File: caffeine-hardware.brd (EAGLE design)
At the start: 65 x 56.5 mm, 31 parts, among them K1 PIN20X2, U1 EEPROM24

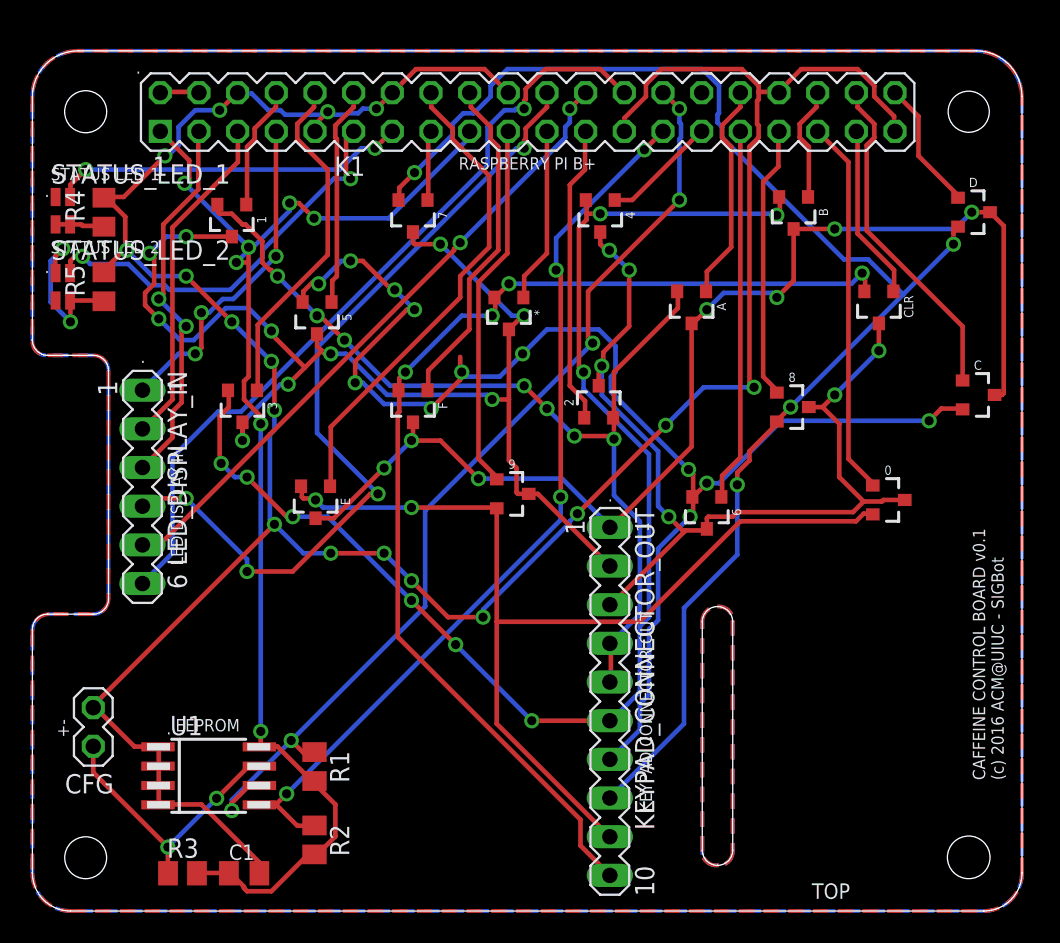
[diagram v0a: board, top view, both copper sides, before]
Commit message: using decoders
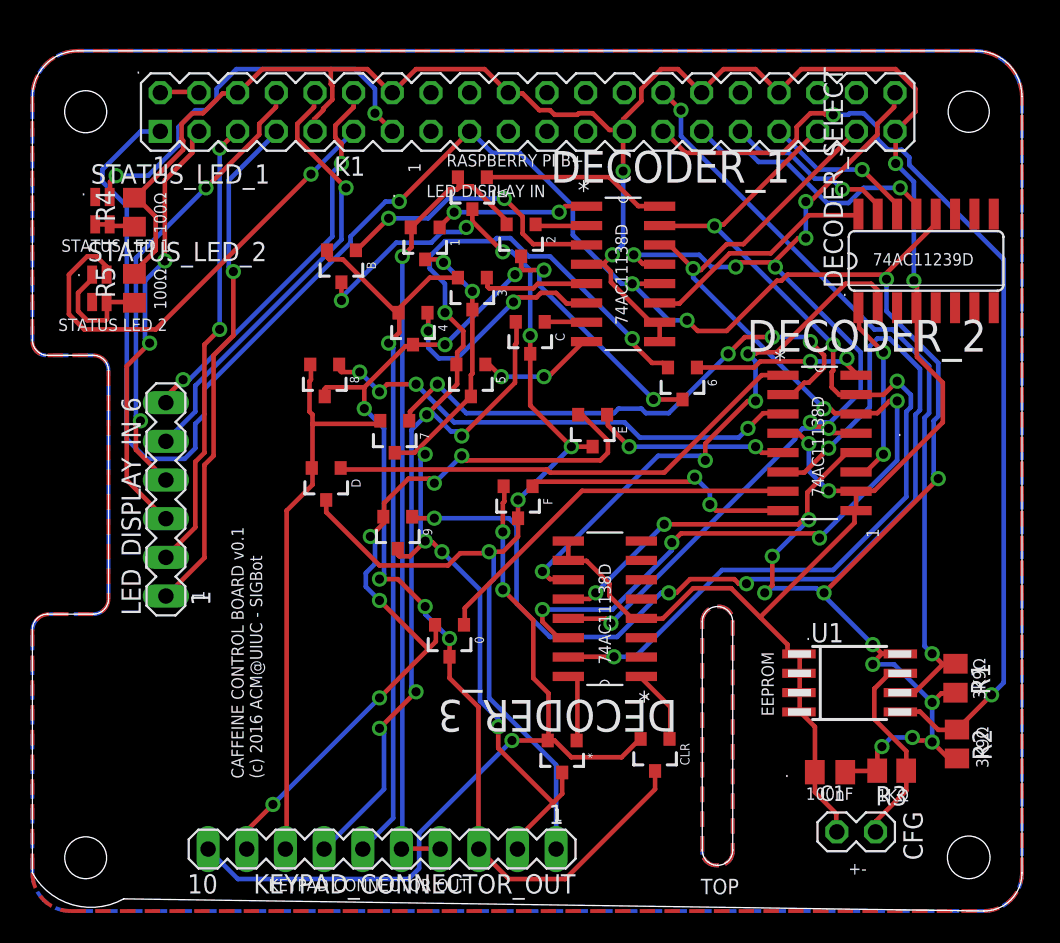
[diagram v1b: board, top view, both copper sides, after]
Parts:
- added DECODER_1, DECODER_2, DECODER_3: 74AC11138D, Texas Instruments_By_element14_Batch_1:SOIC127P600X175-16N
- added DECODER_SELECT: 74AC11239D, 74ac-logic:SO16
- moved CFG 51.7 mm to (55.4, 5.20), turned to 270 degrees
- moved R3 47.1 mm to (56.4, 9.22), turned to 180 degrees
- moved D 46.1 mm to (19.3, 28.1), turned to 180 degrees
- moved R2 42.7 mm to (60.7, 11.0)
- moved U1 42.5 mm to (53.7, 15.0)
- moved R1 42.5 mm to (60.6, 15.3)
- moved C1 39.0 mm to (52.4, 9.12), turned to 180 degrees
- moved CLR 32.9 mm to (40.9, 10.3)
- moved 8 30.8 mm to (19.2, 34.9), turned to 180 degrees
- moved 0 30.2 mm to (27.4, 17.8), turned to 180 degrees
- moved B 29.9 mm to (20.3, 42.4)
- moved C 29.6 mm to (32.7, 37.7), turned to 180 degrees
- moved * 29.3 mm to (34.8, 10.2)
- moved E 18.8 mm to (36.8, 31.6)
- moved KEYPAD_CONNECTOR_OUT 17.8 mm to (23.0, 4.07), turned to 180 degrees
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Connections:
- removed net N$21: 9.1, K1.19
- removed net N$8 (its old number): CLR.1, K1.37
- new net N$10: DECODER_1.11, DECODER_SELECT.16
- new net N$43: 6.1, DECODER_2.16
- new net N$44: D.1, DECODER_2.1
- new net N$45: 7.1, DECODER_2.2
- new net N$46: 8.1, DECODER_2.3
- new net N$47: DECODER_2.5, E.1
- new net N$48: 9.1, DECODER_2.6
- new net N$49: 0.1, DECODER_2.7
- new net N$50: DECODER_2.8, F.1
- new net N$51: *.1, DECODER_3.16
- new net N$52: CLR.1, DECODER_3.1
- net +3V3: now also DECODER_1.12, DECODER_2.12, DECODER_3.12, DECODER_SELECT.12
- net GND: now also DECODER_1.10, DECODER_1.4, DECODER_1.9, DECODER_2.10, DECODER_2.4, DECODER_2.9, DECODER_3.10, DECODER_3.4, DECODER_3.9, DECODER_SELECT.4
- net N$14: now also DECODER_SELECT.14, K1.33; no longer 0.1, K1.35
- net N$15: now also DECODER_1.15, DECODER_2.15, DECODER_3.15, K1.35; no longer 8.1, K1.33
- net N$16: now also DECODER_1.14, DECODER_2.14, DECODER_3.14, K1.37; no longer 6.1, K1.31
- net N$17: now also DECODER_1.13, DECODER_2.13, DECODER_3.13, K1.40; no longer 4.1, K1.29
- net N$18: now also DECODER_SELECT.15, K1.31; no longer 2.1, K1.23
- net N$19: now also DECODER_2.11, DECODER_SELECT.1; no longer 7.1, K1.15
- net N$20: now also DECODER_3.11, DECODER_SELECT.2; no longer *.1, K1.21
- net N$22: now also DECODER_SELECT.13, K1.29; no longer 1.1, K1.8
- net N$23: now also A.1, DECODER_1.16; no longer 3.1, K1.10
- net N$24: now also 1.1, DECODER_1.1; no longer 5.1, K1.12
- net N$25: now also 2.1, DECODER_1.2; no longer F.1, K1.18
- net N$26: now also B.1, DECODER_1.3; no longer E.1, K1.16
- net N$27: now also 3.1, DECODER_1.5; no longer A.1, K1.32
- net N$28: now also 4.1, DECODER_1.6; no longer B.1, K1.36
- net N$29: now also DECODER_1.7; no longer K1.38
- net N$30: now also 5.1, DECODER_1.8; no longer D.1, K1.40
- net N$33: now also K1.8; no longer K1.22
- net N$35: now also K1.12; no longer K1.26
- net N$36: now also K1.10; no longer K1.24
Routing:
- net +3V3: track 85.1 -> 186.5 mm, vias 7 -> 17
- net N$48: track 0.00 -> 68.0 mm, vias 0 -> 4
- net N$17: track 7.76 -> 67.7 mm, vias 0 -> 8
- net N$8: track 93.1 -> 37.5 mm, vias 4 -> 0
- net N$15: track 18.2 -> 66.4 mm, vias 0 -> 4
- net N$16: track 24.6 -> 70.3 mm, vias 0 -> 6
- net N$13: track 89.3 -> 48.2 mm, vias 9 -> 1
- net N$45: track 0.00 -> 36.5 mm, vias 0 -> 4
- net N$46: track 0.00 -> 32.5 mm, vias 0 -> 4
- net N$44: track 0.00 -> 31.9 mm
- net N$35: track 52.1 -> 26.0 mm, vias 1 -> 2
- net N$49: track 0.00 -> 25.2 mm
- net N$20: track 11.6 -> 36.5 mm, vias 0 -> 4
- net N$5: track 78.7 -> 53.8 mm, vias 10 -> 6
- net N$33: track 54.8 -> 30.3 mm, vias 4 -> 2
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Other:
- outline, holes or cut-outs redrawn
- board text added: "100nF"
- board text added: "100Ω"
- board text added: "1KΩ"
- board text added: "3K9Ω"
- board text added: "74AC11138D"
- board text added: "74AC11239D"

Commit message: using n channel
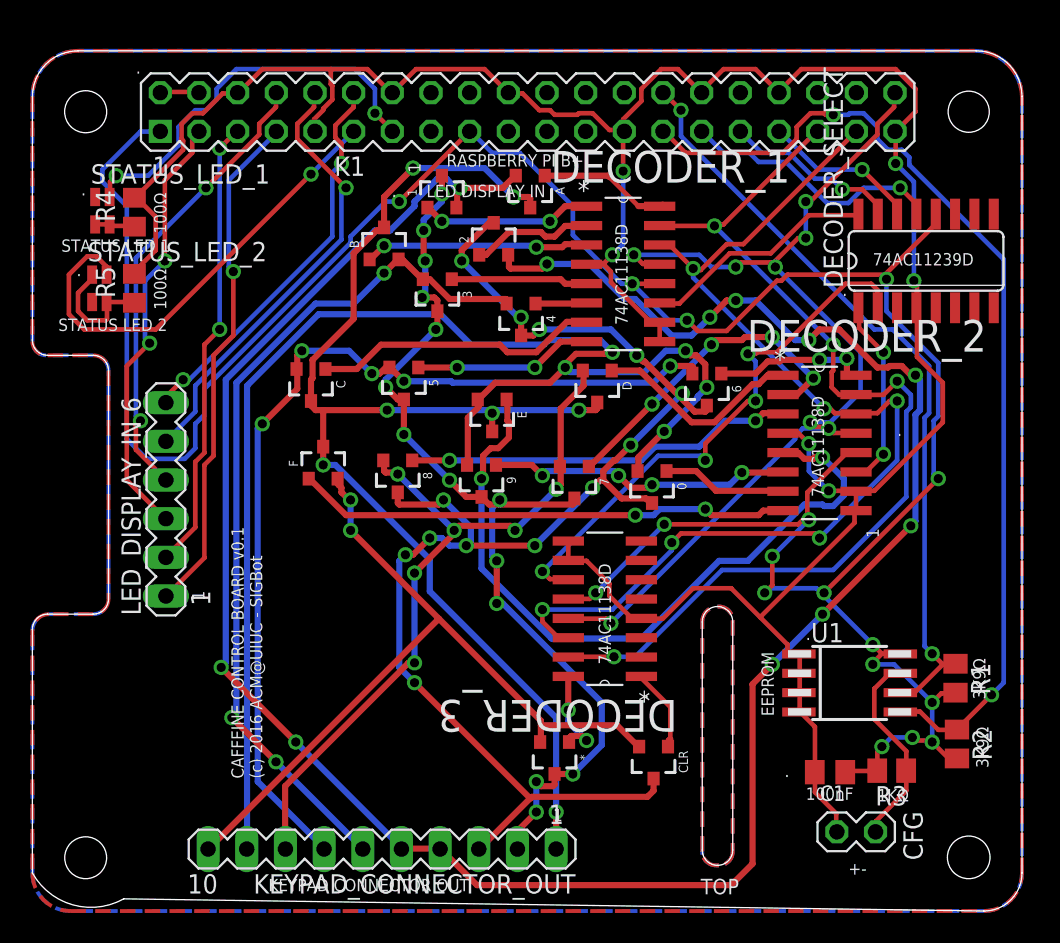
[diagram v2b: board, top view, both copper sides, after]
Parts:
- *, 0, 1, 2, 3, 4, 5, 6, 7, 8, 9, A, B, C, CLR, D, E, F: value BSS84L -> BSS138_F085
- moved D 18.9 mm to (37.1, 34.5)
- moved 0 16.7 mm to (40.7, 27.9)
- moved C 14.7 mm to (18.3, 34.6)
- moved F 13.0 mm to (19.1, 29.4), turned to 0 degrees
- moved 7 12.2 mm to (35.6, 28.2)
- moved 8 7.92 mm to (24.0, 28.6)
- moved 4 7.13 mm to (32.1, 38.9)
- moved E 6.68 mm to (30.2, 32.6)
- moved 9 6.47 mm to (29.5, 28.3)
- moved 5 4.40 mm to (24.4, 34.7)
- moved A 3.80 mm to (32.7, 47.3)
- moved 1 3.48 mm to (26.9, 47.2), turned to 0 degrees
- moved B 3.13 mm to (23.1, 43.8), turned to 0 degrees
- moved 3 2.30 mm to (26.6, 40.5)
- moved 2 1.80 mm to (30.3, 44.1), turned to 0 degrees
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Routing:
- net N$9: track 53.1 -> 157.3 mm, vias 1 -> 11
- net N$48: track 68.0 -> 20.1 mm
- net N$11: track 52.0 -> 91.8 mm, vias 6 -> 5
- net N$47: track 13.0 -> 47.8 mm
- net N$44: track 31.9 -> 13.9 mm
- net N$49: track 25.2 -> 8.19 mm
- net N$29: track 2.75 -> 19.0 mm
- net N$45: track 36.5 -> 21.9 mm
- net N$50: track 18.2 -> 32.6 mm
- net N$7: track 76.0 -> 63.7 mm, vias 6 -> 5
- net N$8: track 37.5 -> 49.5 mm, vias 0 -> 6
- net N$28: track 15.1 -> 3.36 mm, vias 2 -> 0
- net N$6: track 83.1 -> 94.1 mm, vias 8 -> 13
- net N$5: track 53.8 -> 64.8 mm, vias 6 -> 14
- net N$13: track 48.2 -> 56.8 mm, vias 1 -> 3
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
